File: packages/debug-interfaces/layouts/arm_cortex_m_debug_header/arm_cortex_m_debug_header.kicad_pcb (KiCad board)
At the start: 2 copper layers, 1 part

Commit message: Update build script and regenerate outputs
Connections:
- X1 pad 10: line-4 -> line-2
- X1 pad 2: line-2 -> line
- X1 pad 4: line -> line-4
- X1 pad 8: line-3 -> line-5
- X1 pad 9: line-5 -> line-3
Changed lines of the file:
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@@
     )
     (net 0 "")
-    (net 1 "line")
-    (net 2 "line-4")
+    (net 1 "line-4")
+    (net 2 "line-2")
     (net 3 "net")
-    (net 4 "line-3")
-    (net 5 "line-2")
+    (net 4 "line-5")
+    (net 5 "line")
     (net 6 "line-1")
     (net 7 "hv")
-    (net 8 "line-5")
+    (net 8 "line-3")
     (net 9 "gnd")
     (footprint "atopile:CONN-SMD_FTSH-105-01-L-DV-K-TR-c0d174"
@@
             (size 0.9 3)
             (layers "F.Cu" "F.Paste" "F.Mask")
-            (net 1 "line")
+            (net 1 "line-4")
         )
         (pad "3" smd rect
@@
             (size 0.9 3)
             (layers "F.Cu" "F.Paste" "F.Mask")
-            (net 5 "line-2")
+            (net 5 "line")
         )
         (pad "1" smd rect
@@
             (size 0.9 3)
             (layers "F.Cu" "F.Paste" "F.Mask")
-            (net 2 "line-4")
+            (net 2 "line-2")
         )
         (pad "9" smd rect
@@
             (size 0.9 3)
             (layers "F.Cu" "F.Paste" "F.Mask")
-            (net 8 "line-5")
+            (net 8 "line-3")
         )
         (pad "8" smd rect
@@
             (size 0.9 3)
             (layers "F.Cu" "F.Paste" "F.Mask")
-            (net 4 "line-3")
+            (net 4 "line-5")
         )
         (pad "7" smd rect

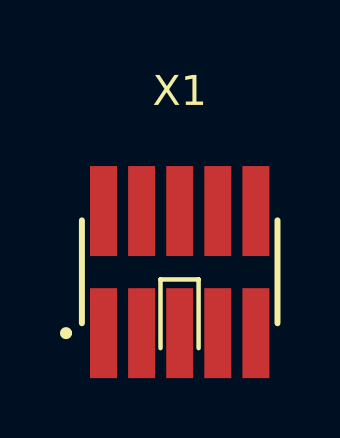
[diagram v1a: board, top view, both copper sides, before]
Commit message: Build all packages without designators on silkscreen.
Also disable fail_on_drc and enable keep_picked_parts for build
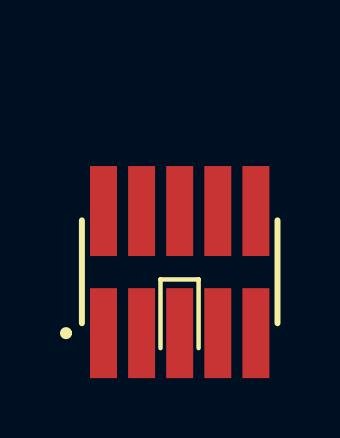
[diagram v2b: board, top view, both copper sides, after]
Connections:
- X1 pad 10: line-2 -> line-1
- X1 pad 2: line -> line-2
- X1 pad 6: line-1 -> line-3
- X1 pad 9: line-3 -> line
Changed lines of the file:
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@@
     (net 0 "")
     (net 1 "line-4")
-    (net 2 "line-2")
+    (net 2 "line-1")
     (net 3 "net")
     (net 4 "line-5")
-    (net 5 "line")
-    (net 6 "line-1")
+    (net 5 "line-2")
+    (net 6 "line-3")
     (net 7 "hv")
-    (net 8 "line-3")
+    (net 8 "line")
     (net 9 "gnd")
     (footprint "atopile:CONN-SMD_FTSH-105-01-L-DV-K-TR-c0d174"
@@
             (at 0 -6.029999999999999 0)
             (layer "F.SilkS")
-            (hide no)
+            (hide yes)
             (effects
                 (font
@@
                     (thickness 0.15)
                 )
+                (hide yes)
             )
             (unlocked no)
@@
             (size 0.9 3)
             (layers "F.Cu" "F.Paste" "F.Mask")
-            (net 5 "line")
+            (net 5 "line-2")
         )
         (pad "1" smd rect
@@
             (size 0.9 3)
             (layers "F.Cu" "F.Paste" "F.Mask")
-            (net 2 "line-2")
+            (net 2 "line-1")
         )
         (pad "9" smd rect
@@
             (size 0.9 3)
             (layers "F.Cu" "F.Paste" "F.Mask")
-            (net 8 "line-3")
+            (net 8 "line")
         )
         (pad "8" smd rect
@@
             (size 0.9 3)
             (layers "F.Cu" "F.Paste" "F.Mask")
-            (net 6 "line-1")
+            (net 6 "line-3")
         )
         (pad "5" smd rect

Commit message: [Publish] Fix image links and rebuild
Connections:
- X1 pad 10: line-1 -> line-2
- X1 pad 2: line-2 -> line-1
- X1 pad 4: line-4 -> line-3
- X1 pad 6: line-3 -> line
- X1 pad 8: line-5 -> line-4
- X1 pad 9: line -> line-5
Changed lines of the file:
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@@
     )
     (net 0 "")
-    (net 1 "line-4")
-    (net 2 "line-1")
+    (net 1 "line-3")
+    (net 2 "line-2")
     (net 3 "net")
-    (net 4 "line-5")
-    (net 5 "line-2")
-    (net 6 "line-3")
+    (net 4 "line-4")
+    (net 5 "line-1")
+    (net 6 "line")
     (net 7 "hv")
-    (net 8 "line")
+    (net 8 "line-5")
     (net 9 "gnd")
     (footprint "atopile:CONN-SMD_FTSH-105-01-L-DV-K-TR-c0d174"
@@
             (size 0.9 3)
             (layers "F.Cu" "F.Paste" "F.Mask")
-            (net 1 "line-4")
+            (net 1 "line-3")
         )
         (pad "3" smd rect
@@
             (size 0.9 3)
             (layers "F.Cu" "F.Paste" "F.Mask")
-            (net 5 "line-2")
+            (net 5 "line-1")
         )
         (pad "1" smd rect
@@
             (size 0.9 3)
             (layers "F.Cu" "F.Paste" "F.Mask")
-            (net 2 "line-1")
+            (net 2 "line-2")
         )
         (pad "9" smd rect
@@
             (size 0.9 3)
             (layers "F.Cu" "F.Paste" "F.Mask")
-            (net 8 "line")
+            (net 8 "line-5")
         )
         (pad "8" smd rect
@@
             (size 0.9 3)
             (layers "F.Cu" "F.Paste" "F.Mask")
-            (net 4 "line-5")
+            (net 4 "line-4")
         )
         (pad "7" smd rect
@@
             (size 0.9 3)
             (layers "F.Cu" "F.Paste" "F.Mask")
-            (net 6 "line-3")
+            (net 6 "line")
         )
         (pad "5" smd rect
